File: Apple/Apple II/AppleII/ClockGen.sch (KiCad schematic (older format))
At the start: 23 parts, among them Q1 2N4258, Q2 2N4258, Y1 XT0001

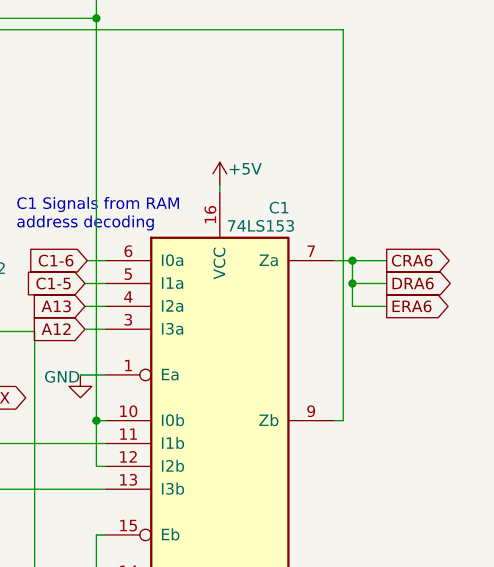
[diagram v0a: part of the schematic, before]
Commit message: Created separate II and II+ projects, stated updating the II+
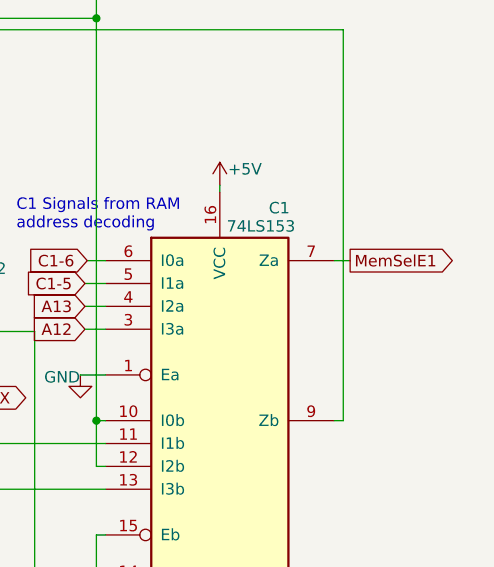
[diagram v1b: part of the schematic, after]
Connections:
- net CRA6 renamed MemSelE1
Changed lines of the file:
@@
 encoding utf-8
 Sheet 5 9
-Title "Apple II+ Schematic"
+Title "Apple II Schematic"
 Date ""
 Rev "0"
@@
 Text Notes 9330 4480 0    50   ~ 0
 C1 Signals from RAM\naddress decoding
+Text GLabel 10790 4610 2    50   Output ~ 0
+MemSelE1
+Wire Wire Line
+	10790 4610 10720 4610
 Text Notes 5850 6860 0    50   ~ 0
 Horizontal Video Address
@@
 Wire Notes Line
 	3310 2020 4120 2020
-Text GLabel 10950 4610 2    50   Output ~ 0
-CRA6
-Text GLabel 10950 4710 2    50   Output ~ 0
-DRA6
-Text GLabel 10950 4810 2    50   Output ~ 0
-ERA6
-Wire Wire Line
-	10800 4710 10950 4710
-Wire Wire Line
-	10800 4810 10950 4810
-Wire Wire Line
-	10720 4610 10800 4610
-Wire Wire Line
-	10800 4610 10800 4710
-Connection ~ 10800 4610
-Wire Wire Line
-	10800 4610 10950 4610
-Wire Wire Line
-	10800 4810 10800 4710
 Wire Bus Line
 	5910 2770 5910 4910
@@
 Wire Bus Line
 	5790 870  5790 3180
-Connection ~ 10800 4710
 $EndSCHEMATC
